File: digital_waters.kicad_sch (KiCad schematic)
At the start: 12 parts, among them J12 SLOT 2, J13 SLOT 1

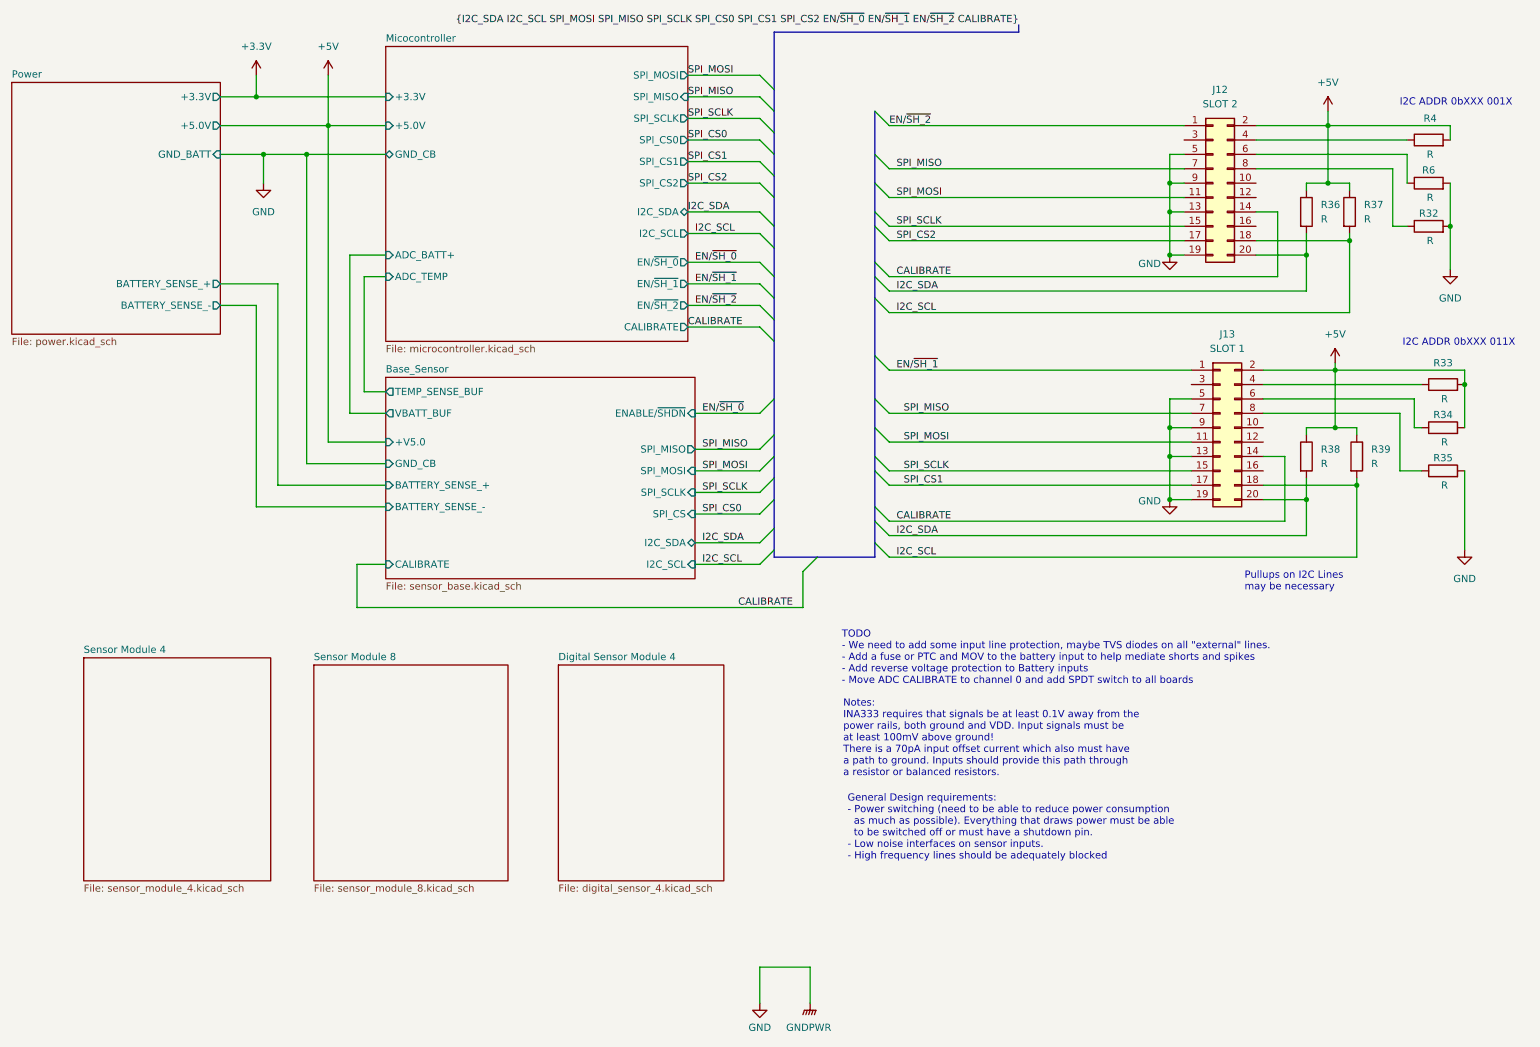
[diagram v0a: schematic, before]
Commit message: Began assigning footprints Cleaned up some of the signalling and added the full prototype sensor suite Added a header for the Atlas Scientific carrier board Added some test points and jumpers Cleaned up the power section Started work on the CPU signal assignment and header sockets
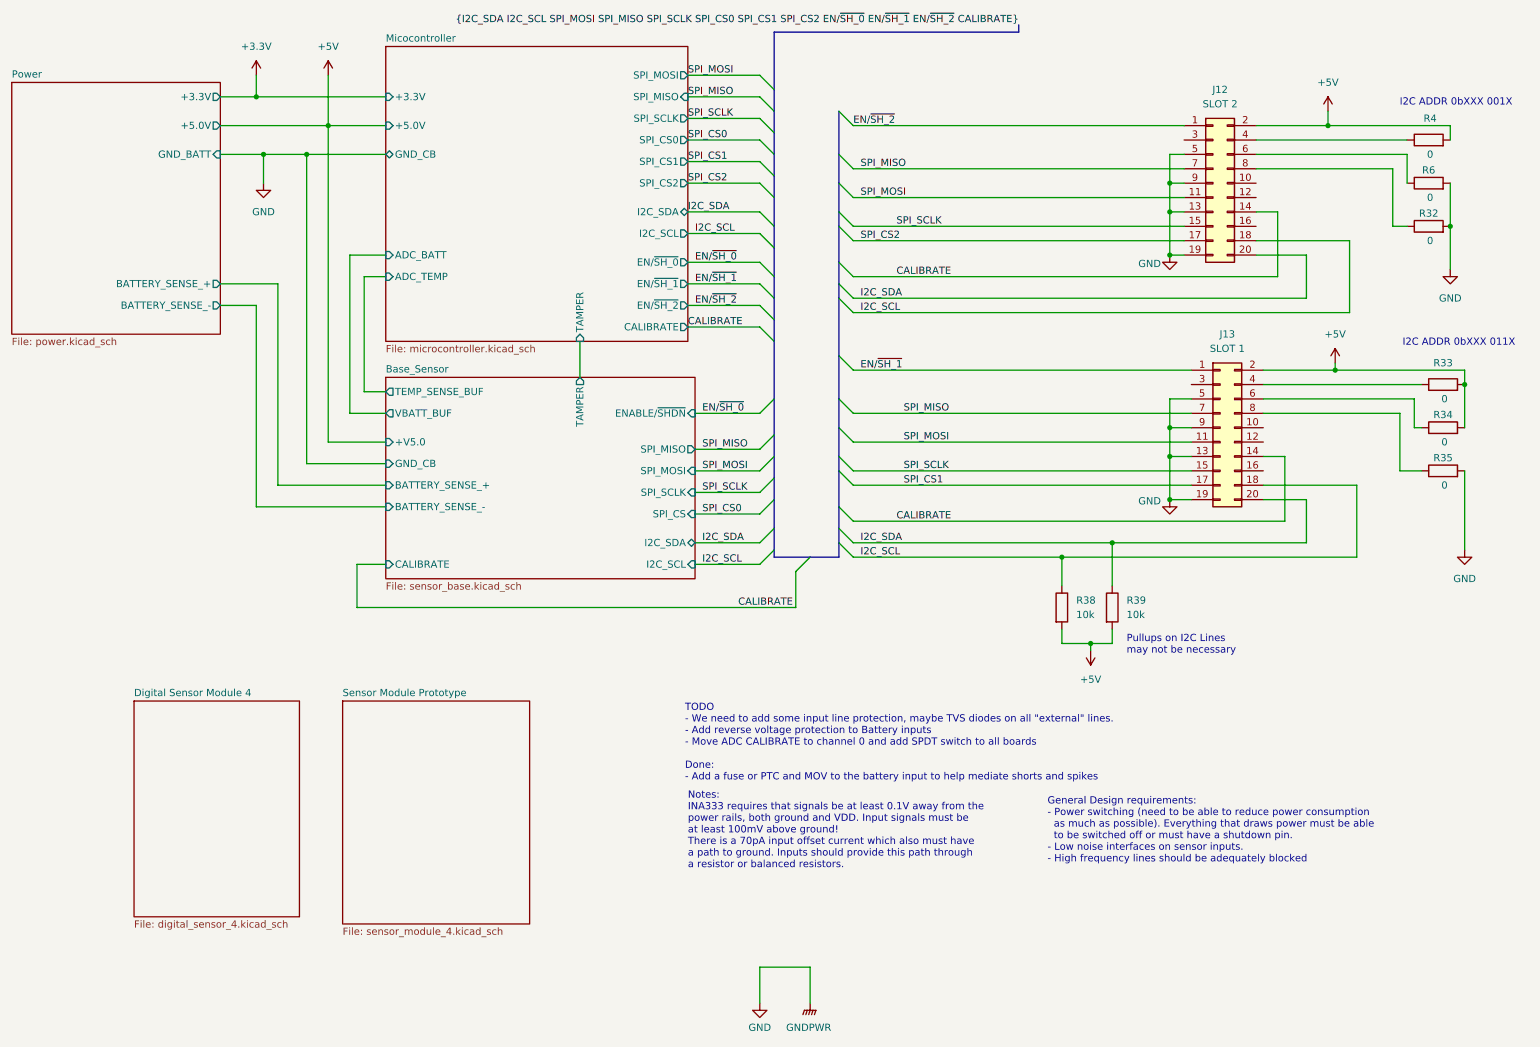
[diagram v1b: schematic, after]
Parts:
- removed R36, R37: R, symbol Device:R
- R32, R33, R34, R35, R4, R6: value R -> 0
- R38, R39: value R -> 10k
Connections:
- net +5V: now also R38.2, R39.2; no longer R38.1, R39.1
- net I2C_SCL: now also R38.1; no longer R39.2
- net I2C_SDA: now also R39.1; no longer R38.2
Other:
- sheet Sensor Module 4 renamed Sensor Module Prototype
- removed sheet Sensor Module 8
- sheet Base_Sensor ports: added TAMPER; removed none
- sheet Micocontroller ports: added ADC_BATT, TAMPER; removed ADC_BATT+
- note added: "Pullups on I2C Lines may not be necessary"
- note added: "TODO - We need to add some input line protection, maybe TVS diodes on all "external" lines. - Add reverse voltage protection to Battery inputs - Move ADC CALIBRATE to channel 0 and add SPDT switch to all boards Done: - Add a fuse or PTC and MOV to the battery input to help mediate shorts and spikes"
- note removed: "Pullups on I2C Lines may be necessary"
- note removed: "TODO - We need to add some input line protection, maybe TVS diodes on all "external" lines. - Add a fuse or PTC and MOV to the battery input to help mediate shorts and spikes - Add reverse voltage protection to Battery inputs - Move ADC CALIBRATE to channel 0 and add SPDT switch to all boards"
- moved on the sheet: R38, R39
